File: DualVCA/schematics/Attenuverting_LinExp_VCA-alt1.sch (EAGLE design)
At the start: 247 parts, among them IC1 TL074D, IC10 TL074D, IC11 TL072D, IC12 QUAD_OPAMPD, IC14 QUAD_OPAMPD, IC2 SSM2164S, IC3 TL074D, IC4 TL072D, IC5 TL074D, IC6 SSM2164S, IC7 TL074D, IC8 TL074D, IC9 TL074D, Q1 BC856ALT1SMD, Q10 BSS123, Q2 BC856ALT1SMD, Q3 BC856ALT1SMD, Q5 BC856ALT1SMD, Q9 BSS84

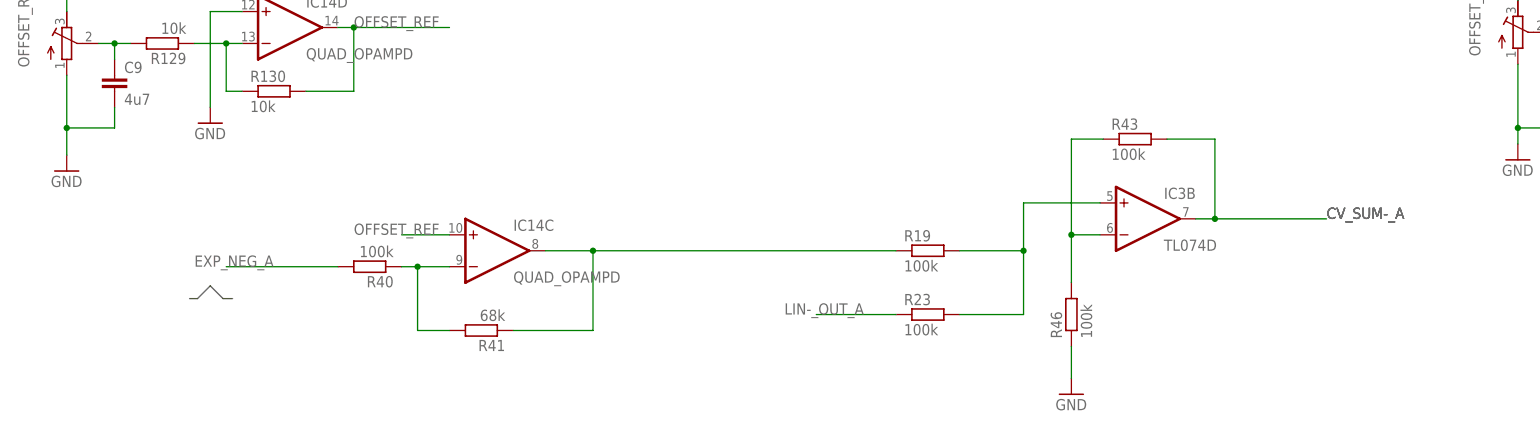
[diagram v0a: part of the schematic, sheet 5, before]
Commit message: updated negative summing A circuit
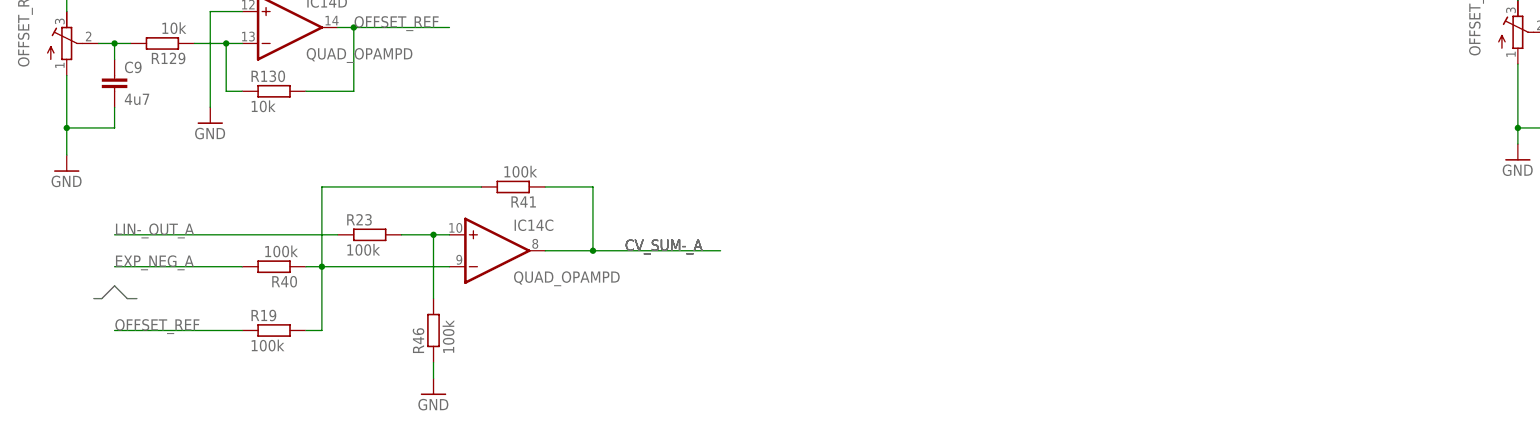
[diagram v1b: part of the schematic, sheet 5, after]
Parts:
- removed R43: 100k, Rebel:R-EU_0603
- R41: value 68k -> 100k
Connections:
- removed net EXP_NEG: IC14C.OUT, R19.1, R41.1
- removed net N$1: IC3B.+IN, R19.2, R23.2
- removed net N$3: IC3B.-IN, R43.1, R46.2
- new net N$8: IC14C.+IN, R23.2, R46.2
- net CV_SUM-_A: now also IC14C.OUT, R41.1; no longer IC3B.OUT, R43.2
- net N$41: now also R19.2
- net OFFSET_REF: now also R19.1; no longer IC14C.+IN
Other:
- moved on the sheet: R19, R23, R40, R41, R46
